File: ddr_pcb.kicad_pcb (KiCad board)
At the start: 2 copper layers, 17 parts, among them J1 Screw_Terminal_01x04, J2 Screw_Terminal_01x04, J3 Screw_Terminal_01x04, J4 Screw_Terminal_01x06, J5 Screw_Terminal_01x04, U1 ProMicro

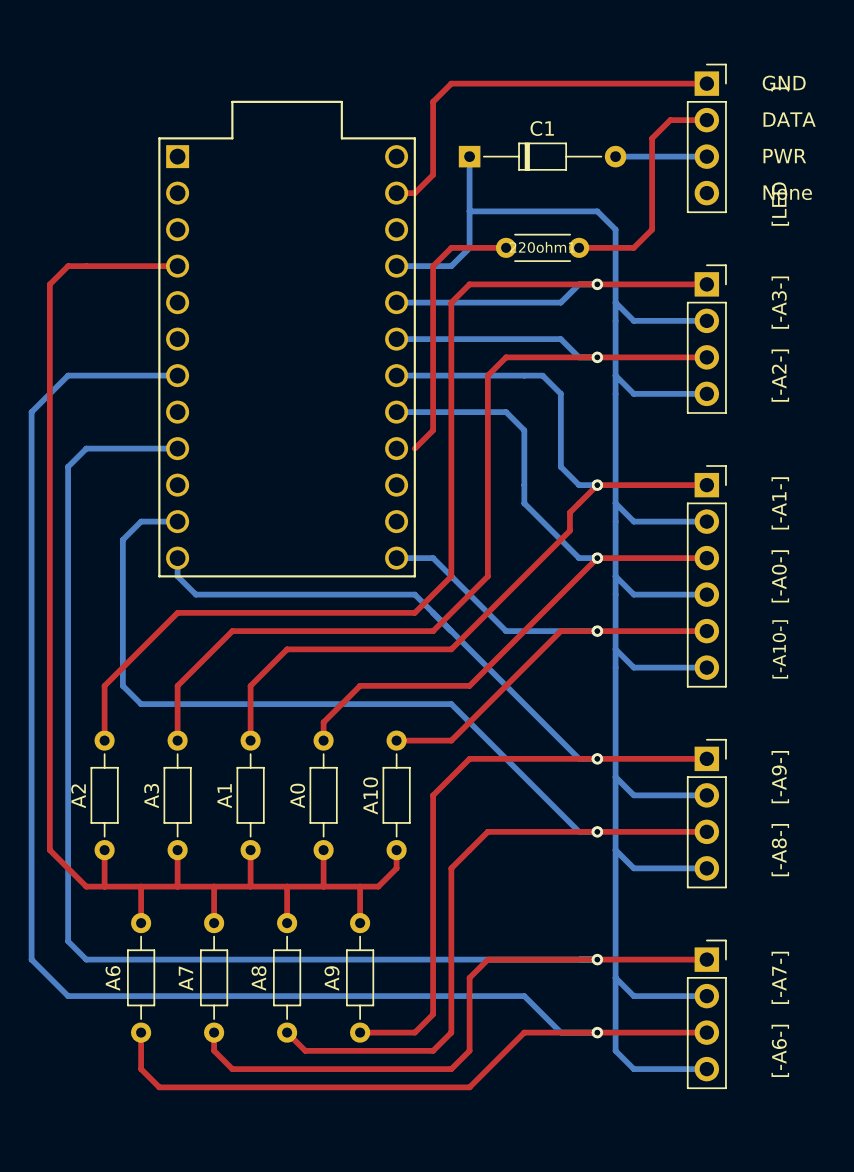
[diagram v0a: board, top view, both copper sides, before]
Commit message: new: add bigger holes for resistors so that we can socket them
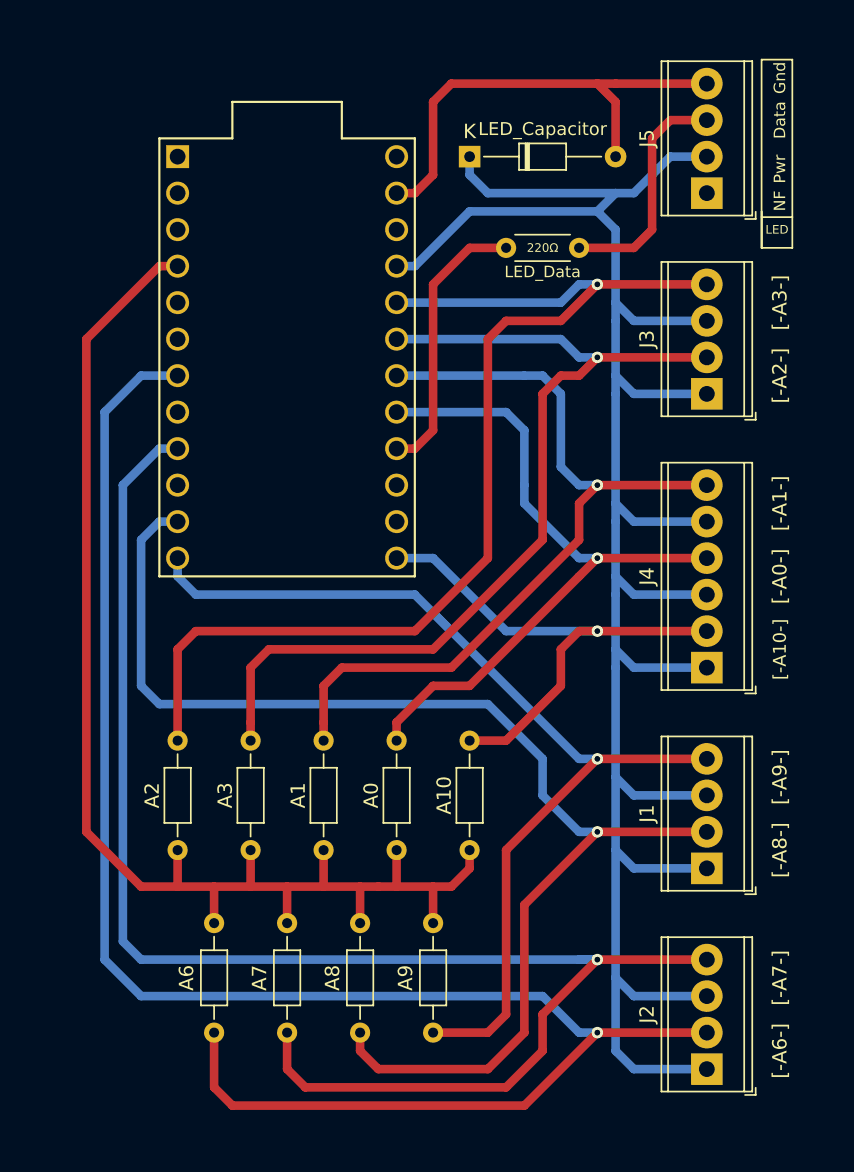
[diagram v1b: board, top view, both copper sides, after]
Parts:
- J1, J2, J3, J5: footprint Connector_PinSocket_2.54mm:PinSocket_1x04_P2.54mm_Vertical -> TerminalBlock_Phoenix:TerminalBlock_Phoenix_MPT-0,5-4-2.54_1x04_P2.54mm_Horizontal
- J4: footprint Connector_PinSocket_2.54mm:PinSocket_1x06_P2.54mm_Vertical -> TerminalBlock_Phoenix:TerminalBlock_Phoenix_MPT-0,5-6-2.54_1x06_P2.54mm_Horizontal
- moved J4 12.7 mm to (114.3, 111.8), turned to 90 degrees
- moved J1 7.62 mm to (114.3, 125.7), turned to 90 degrees
- moved J3 7.62 mm to (114.3, 92.7), turned to 90 degrees
- moved J5 7.62 mm to (114.3, 78.7), turned to 90 degrees
- moved J2 7.62 mm to (114.3, 139.7), turned to 90 degrees
- moved A10 5.08 mm to (97.8, 116.8)
- moved A0 5.08 mm to (92.7, 116.8)
- moved A1 5.08 mm to (87.6, 116.8)
- moved A2 5.08 mm to (77.5, 116.8)
- moved A3 5.08 mm to (82.5, 116.8)
- moved A6 5.08 mm to (80.0, 137.2)
- moved A7 5.08 mm to (85.1, 137.2)
- moved A8 5.08 mm to (90.2, 137.2)
- moved A9 5.08 mm to (95.2, 137.2)
- renumbered C1 to LED_Capacitor, 220ohm1 to LED_Data
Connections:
- J1 pad 1: Net-(A9-Pad1) -> Net-(J1-Pad1)
- J1 pad 2: Net-(C1-Pad1) -> Net-(A8-Pad1)
- J1 pad 3: Net-(A8-Pad1) -> Net-(J1-Pad1)
- J1 pad 4: Net-(C1-Pad1) -> Net-(A9-Pad1)
- J2 pad 1: Net-(A7-Pad1) -> Net-(J1-Pad1)
- J2 pad 2: Net-(C1-Pad1) -> Net-(A6-Pad1)
- J2 pad 3: Net-(A6-Pad1) -> Net-(J1-Pad1)
- J2 pad 4: Net-(C1-Pad1) -> Net-(A7-Pad1)
- J3 pad 1: Net-(A2-Pad1) -> Net-(J1-Pad1)
- J3 pad 2: Net-(C1-Pad1) -> Net-(A3-Pad1)
- J3 pad 3: Net-(A3-Pad1) -> Net-(J1-Pad1)
- J3 pad 4: Net-(C1-Pad1) -> Net-(A2-Pad1)
- J4 pad 1: Net-(A1-Pad1) -> Net-(J1-Pad1)
- J4 pad 2: Net-(C1-Pad1) -> Net-(A10-Pad1)
- J4 pad 3: Net-(A0-Pad1) -> Net-(J1-Pad1)
- J4 pad 4: Net-(C1-Pad1) -> Net-(A0-Pad1)
- J4 pad 5: Net-(A10-Pad1) -> Net-(J1-Pad1)
- J4 pad 6: Net-(C1-Pad1) -> Net-(A1-Pad1)
- J5 pad 1: Net-(J5-Pad1) -> (no net)
- J5 pad 2: Net-(220ohm1-Pad1) -> Net-(J1-Pad1)
- J5 pad 3: Net-(C1-Pad2) -> Net-(220ohm1-Pad1)
- J5 pad 4: (no net) -> Net-(J5-Pad4)
- LED_Capacitor pad 1: Net-(C1-Pad1) -> Net-(J1-Pad1)
- LED_Capacitor pad 2: Net-(C1-Pad2) -> Net-(J5-Pad4)
- U1 pad 21: Net-(C1-Pad1) -> Net-(J1-Pad1)
- U1 pad 23: Net-(J5-Pad1) -> Net-(J5-Pad4)
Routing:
- net Net-(J1-Pad1): track 0.00 -> 157.5 mm
- net Net-(C1-Pad1): track 141.7 -> 0.00 mm
- net Net-(J5-Pad4): track 0.00 -> 33.3 mm
- net Net-(J5-Pad1): track 27.7 -> 0.00 mm
- net Net-(A6-Pad1): track 134.8 -> 121.4 mm
- net Net-(A7-Pad1): track 122.0 -> 108.9 mm
- net Net-(A9-Pad1): track 78.5 -> 71.2 mm
- net Net-(A3-Pad1): track 72.8 -> 66.2 mm
- net Net-(C1-Pad2): track 6.35 -> 0.00 mm
- net Net-(A8-Pad1): track 94.5 -> 88.6 mm
- net Net-(A2-Pad1): track 82.9 -> 77.1 mm
- net Net-(A0-Pad1): track 53.8 -> 48.7 mm
- net Net-(A1-Pad1): track 62.2 -> 57.9 mm
- net Net-(A10-Pad1): track 40.8 -> 37.2 mm
- net Net-(A0-Pad2): track 96.1 -> 93.1 mm
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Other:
- net class Default: trace_width 0.4 -> 0.6
- rule trace_min: 0.2 -> 0.6
- board text added: "Data"
- board text added: "Gnd"
- board text added: "LED"
- board text added: "NF"
- board text added: "Pwr"
- board text removed: "DATA"
- board text removed: "GND"
- board text removed: "None"
- board text removed: "PWR"
- board text removed: "[LED ]"

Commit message: Change resistor to have a bigger hole, fix text size
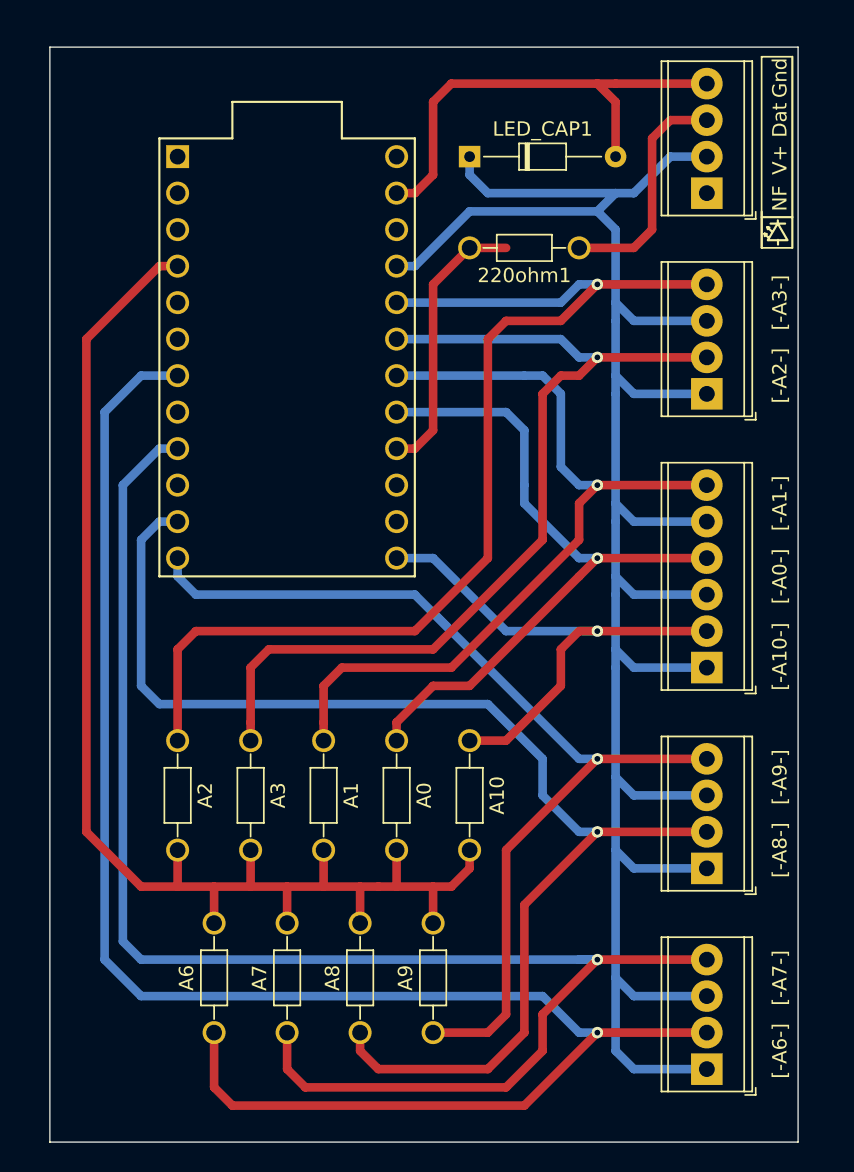
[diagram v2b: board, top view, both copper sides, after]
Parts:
- 220ohm1: renamed from LED_Data; footprint Resistor_THT:R_Axial_DIN0204_L3.6mm_D1.6mm_P5.08mm_Horizontal -> ddr_pcb:R_Axial_DDRPAD_L3.6mm_D1.6mm_P7.62mm_Horizontal
- A0, A1, A10, A2, A3, A6, A7, A8, A9: footprint Resistor_THT:R_Axial_DIN0204_L3.6mm_D1.6mm_P7.62mm_Horizontal -> ddr_pcb:R_Axial_DDRPAD_L3.6mm_D1.6mm_P7.62mm_Horizontal
- renumbered LED_Capacitor to LED_CAP1
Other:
- board outline added: 52.1 x 76.2 mm
- board text added: "Dat"
- board text added: "JLCJLCJLCJLC"
- board text added: "V+"
- board text added: "XeaL's FSR PCB"
- board text removed: "Data"
- board text removed: "LED"
- board text removed: "Pwr"

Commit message: new: Ordered through JLCPCB!
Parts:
- renumbered 220ohm1 to 220Ω, LED_CAP1 to LED_CAP
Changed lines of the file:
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@@
     (38 B.Mask user)
     (39 F.Mask user)
-    (40 Dwgs.User user hide)
+    (40 Dwgs.User user)
     (41 Cmts.User user hide)
     (42 Eco1.User user hide)
@@
     (pcbplotparams
       (layerselection 0x010fc_ffffffff)
-      (usegerberextensions false)
-      (usegerberattributes true)
-      (usegerberadvancedattributes true)
-      (creategerberjobfile true)
+      (usegerberextensions true)
+      (usegerberattributes false)
+      (usegerberadvancedattributes false)
+      (creategerberjobfile false)
       (excludeedgelayer true)
       (linewidth 0.100000)
@@
       (plotinvisibletext false)
       (padsonsilk false)
-      (subtractmaskfromsilk false)
+      (subtractmaskfromsilk true)
       (outputformat 1)
       (mirror false)
@@
     (descr "Resistor, Axial_DIN0204 series, Axial, Horizontal, pin pitch=7.62mm, 0.167W, length*diameter=3.6*1.6mm^2, http://cdn-reichelt.de/documents/datenblatt/B400/1_4W%23YAG.pdf")
     (tags "Resistor Axial_DIN0204 series Axial Horizontal pin pitch 7.62mm 0.167W length 3.6mm diameter 1.6mm")
-    (fp_text reference 220ohm1 (at 3.81 -1.92) (layer F.SilkS)
+    (fp_text reference 220Ω (at 3.7846 0.0508) (layer F.SilkS)
       (effects (font (size 1 1) (thickness 0.15)))
     )
@@
     (descr "Diode, DO-34_SOD68 series, Axial, Horizontal, pin pitch=10.16mm, , length*diameter=3.04*1.6mm^2, , https://www.nxp.com/docs/en/data-sheet/KTY83_SER.pdf")
     (tags "Diode DO-34_SOD68 series Axial Horizontal pin pitch 10.16mm  length 3.04mm diameter 1.6mm")
-    (fp_text reference LED_CAP1 (at 5.08 -1.92) (layer F.SilkS)
-      (effects (font (size 1 1) (thickness 0.15)))
-    )
+    (fp_text reference LED_CAP (at 5.08 -1.92) (layer F.SilkS)
+      (effects (font (size 1 1) (thickness 0.15)))
+    )

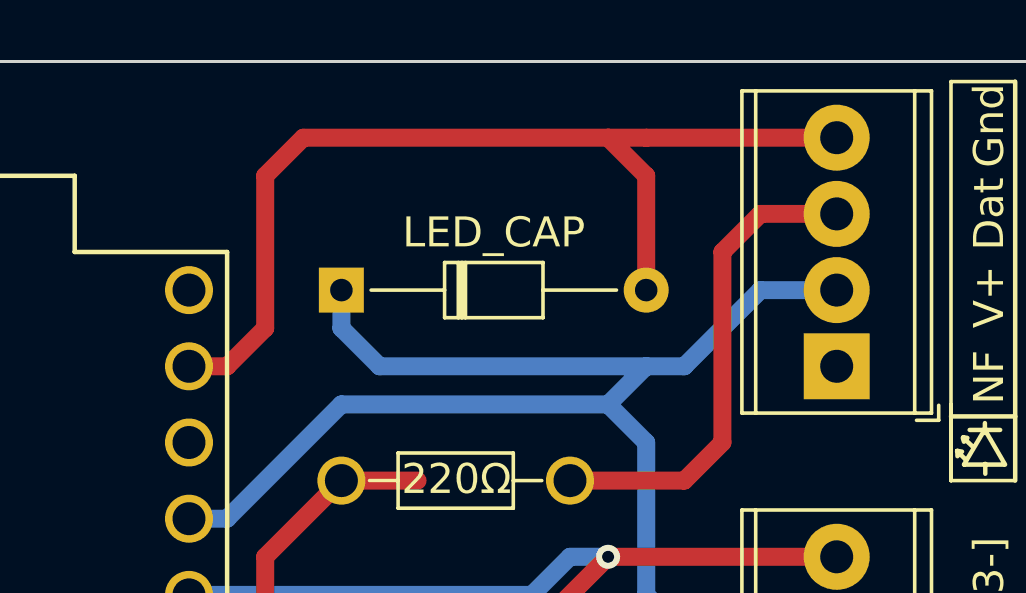
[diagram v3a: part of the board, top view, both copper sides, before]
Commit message: new: Change Capacitor to match real life more
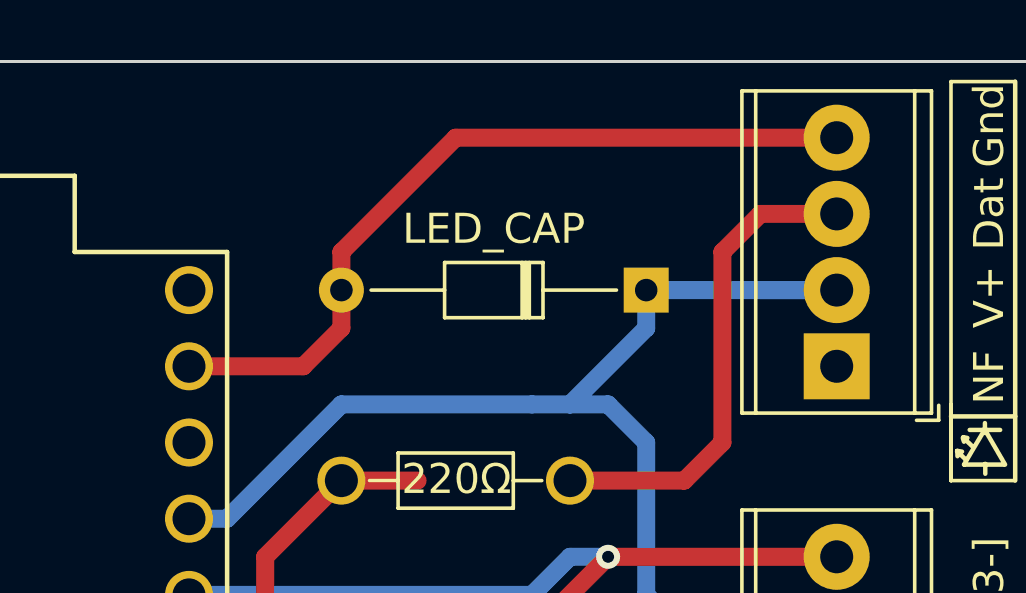
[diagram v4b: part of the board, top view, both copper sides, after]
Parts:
- moved LED_CAP 10.2 mm to (108.0, 76.2), turned to 180 degrees
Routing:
- net Net-(J1-Pad1): track 157.5 -> 150.1 mm
- net Net-(J5-Pad4): track 33.3 -> 26.2 mm

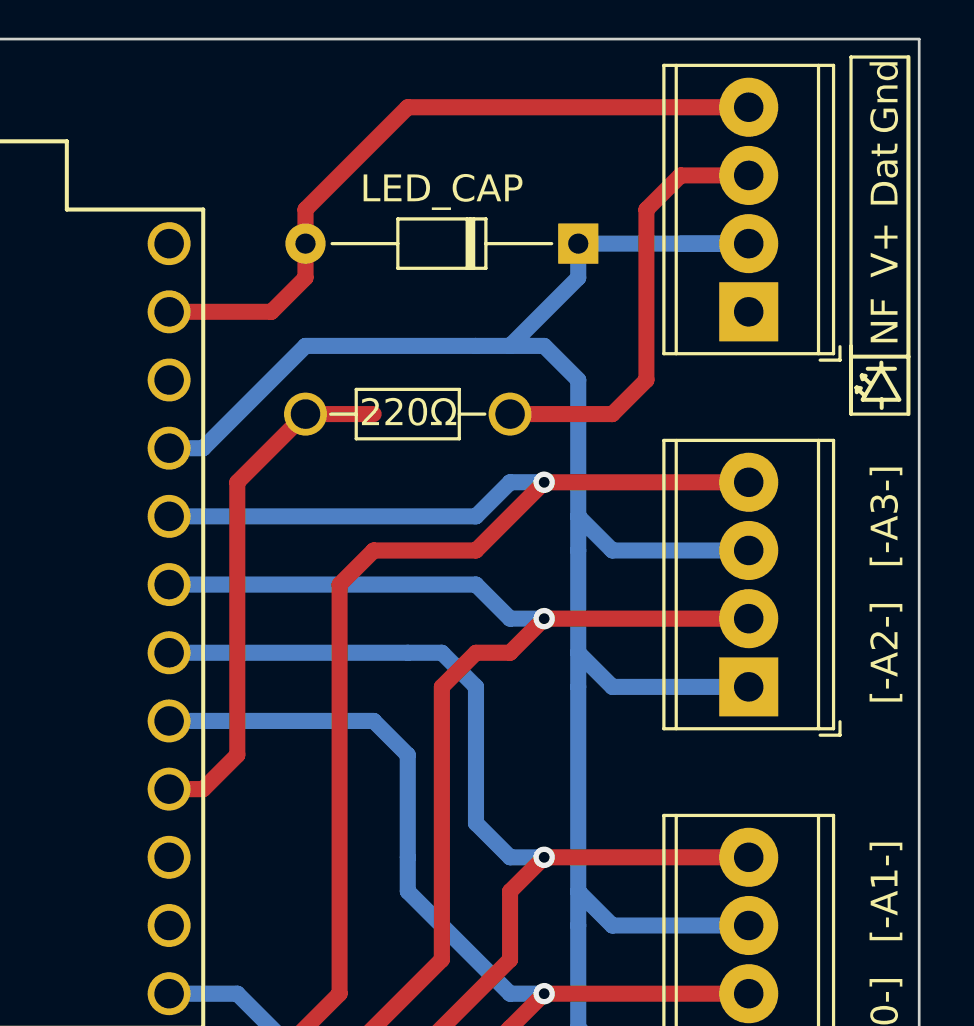
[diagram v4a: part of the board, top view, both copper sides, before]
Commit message: new: Add extra link for APA102
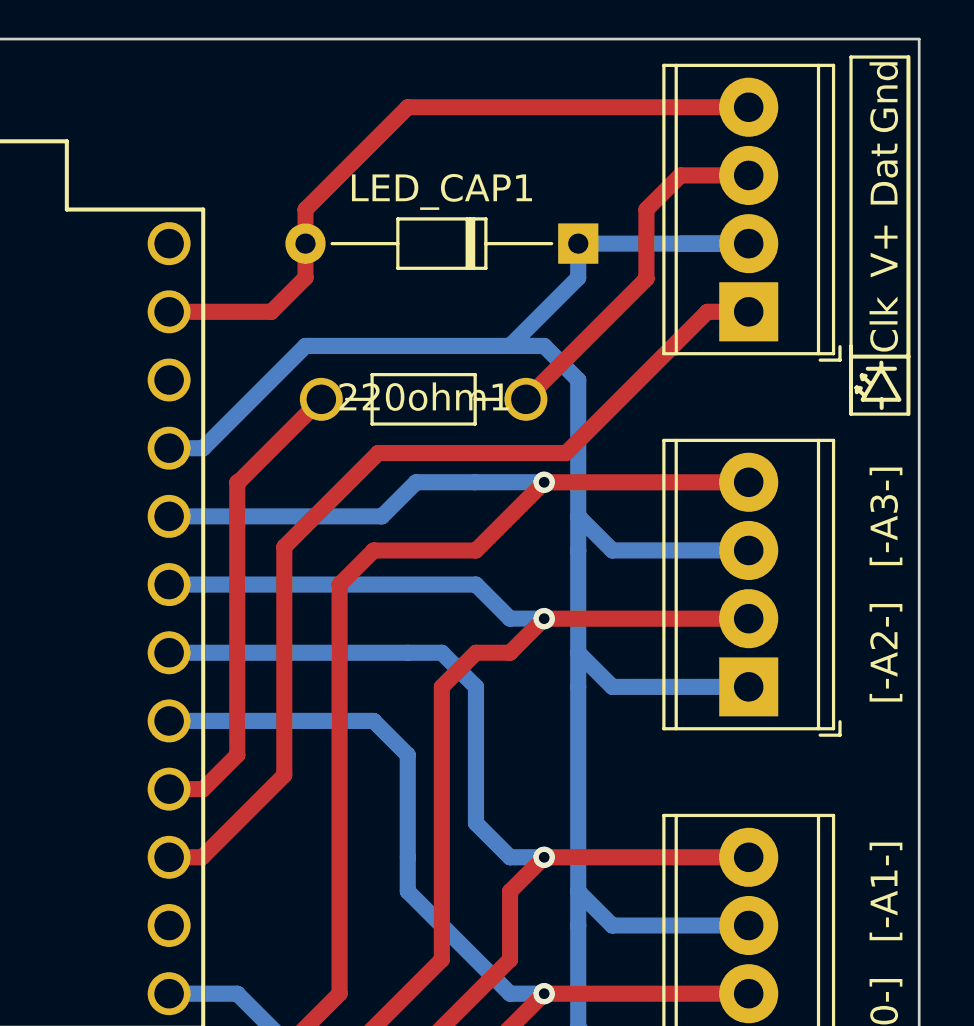
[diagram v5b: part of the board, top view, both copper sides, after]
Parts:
- moved 220ohm1 0.81 mm to (106.0, 82.0)
- renumbered 220Ω to 220ohm1, LED_CAP to LED_CAP1
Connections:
- J5 pad 1: (no net) -> Net-(J5-Pad1)
- U1 pad 15: (no net) -> Net-(J5-Pad1)
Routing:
- net Net-(J5-Pad1): track 0.00 -> 35.0 mm
- net Net-(220ohm1-Pad1): track 16.3 -> 13.3 mm
- net Net-(220ohm1-Pad2): track 19.4 -> 17.6 mm
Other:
- board text added: "Clk"
- board text removed: "NF"

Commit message: new: Leaner and meaner (v2.0)
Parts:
- moved J2 26.1 mm to (96.5, 120.7), turned to 0 degrees
- moved A10 14.8 mm to (85.1, 109.2)
- moved A9 9.94 mm to (90.8, 128.3)
- moved A8 9.44 mm to (87.0, 128.3)
- moved A1 9.16 mm to (92.7, 109.2)
- moved A7 9.09 mm to (83.2, 128.3)
- moved A6 8.91 mm to (79.4, 128.3)
- moved A0 8.52 mm to (88.9, 109.2)
- moved A3 7.73 mm to (81.3, 109.2)
- moved A2 7.62 mm to (77.5, 109.2)
- moved J1 7.18 mm to (109.2, 120.7), turned to 0 degrees
- renumbered 220ohm1 to 220Ω, LED_CAP1 to LED_CAP
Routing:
- net Net-(A6-Pad1): track 121.4 -> 67.0 mm, vias 1 -> 0
- net Net-(A7-Pad1): track 108.9 -> 64.8 mm, vias 1 -> 0
- net Net-(A8-Pad1): track 88.6 -> 65.8 mm, vias 1 -> 0
- net Net-(A0-Pad2): track 93.1 -> 70.8 mm
- net Net-(J1-Pad1): track 150.1 -> 130.6 mm
- net Net-(A1-Pad1): track 57.9 -> 45.9 mm
- net Net-(A10-Pad1): track 37.2 -> 48.4 mm
- net Net-(A9-Pad1): track 71.2 -> 78.4 mm
- net Net-(A2-Pad1): track 77.1 -> 70.7 mm
- net Net-(A3-Pad1): track 66.2 -> 62.0 mm
- net Net-(A0-Pad1): track 48.7 -> 50.8 mm
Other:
- board size 52.1 x 76.2 mm -> 48.7 x 61.6 mm
- board text added: "Version 2.0"
- board text removed: "JLCJLCJLCJLC"
